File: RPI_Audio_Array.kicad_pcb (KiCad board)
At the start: 2 copper layers, 40 parts, among them J1 Conn_02x20_Odd_Even, U1 PCMD3140IRTER, U2 SPH0690LM4H-1, U3 SPH0690LM4H-1, U4 SPH0690LM4H-1, U5 SPH0690LM4H-1, U6 TLV7103318QDSERQ1

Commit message: Fix: Schemtatic fixes
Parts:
- added C21: 2.2uf, Capacitor_SMD:C_0805_2012Metric, F.Cu at (40.0, 84.4)
- added C22: 2.2uf, Capacitor_SMD:C_0805_2012Metric, F.Cu at (40.2, 67.1)
- added C23: 2.2uf, Capacitor_SMD:C_0805_2012Metric, F.Cu at (40.1, 51.6)
- added C24: 2.2uf, Capacitor_SMD:C_0805_2012Metric, F.Cu at (40.6, 37.2)
- added C25: 2.2uf, Capacitor_SMD:C_0805_2012Metric, F.Cu at (64.0, 54.1)
- added C26: 100nf, Capacitor_SMD:C_1206_3216Metric, F.Cu at (71.5, 45.2)
- added C27: 1nf, Capacitor_SMD:C_0805_2012Metric, F.Cu at (67.8, 45.7)
- added C28: 100pf, Capacitor_SMD:C_0805_2012Metric, F.Cu at (65.5, 45.8)
- added C29: 10uf, Capacitor_SMD:C_1206_3216Metric, F.Cu at (74.3, 45.2)
- added R3: 470, Resistor_SMD:R_0201_0603Metric, F.Cu at (70.3, 52.3)
- added R5: 470, Resistor_SMD:R_0201_0603Metric, F.Cu at (68.8, 52.6)
- C13: value 1uf -> 10nf; footprint Capacitor_SMD:C_0603_1608Metric -> Capacitor_SMD:C_01005_0402Metric
- moved J1 45.8 mm to (83.3, 76.1), turned to 180 degrees
- moved C13 4.33 mm to (69.6, 45.8), turned to 90 degrees
- moved C16 3.52 mm to (62.4, 57.0), turned to -90 degrees
- moved C14 3.10 mm to (66.0, 48.5)
- moved R4 2.93 mm to (70.0, 60.3), turned to 90 degrees
- moved C18 2.28 mm to (66.7, 53.4), turned to 180 degrees
- moved C20 2.08 mm to (66.8, 51.1), turned to 90 degrees
- moved FB1 1.92 mm to (64.3, 51.2), turned to -90 degrees
- moved C17 1.42 mm to (64.0, 56.5), turned to -90 degrees
- moved C15 1.16 mm to (61.4, 50.8)
- moved C19 0.74 mm to (65.0, 56.5), turned to 90 degrees
- moved U6 0.66 mm to (63.0, 47.6)
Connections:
- net GPIO1 renamed PCMD_GPIO1
- C14 pad 1: AVDD -> IOVDD
- FB1 pad 1: AVDD -> IOVDD
- FB1 pad 2: GND -> AVDD
- U1 pad 9: AVDD -> IOVDD
- U2 pad 2: VDD -> IOVDD
- U4 pad 2: VDD -> IOVDD
- U6 pad 6: AVDD -> IOVDD
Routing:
- net PDMCLK: track 134.0 -> 13.9 mm
- net PDM_IN_2: track 69.0 -> 2.48 mm
- net PDM_IN_1: track 65.7 -> 2.69 mm
- net +5V: track 27.1 -> 50.5 mm
- net IOVDD: track 0.00 -> 22.5 mm, vias 0 -> 4
- net AVDD: track 15.5 -> 4.16 mm, vias 2 -> 0
- net SDOUT: track 23.4 -> 33.7 mm, vias 0 -> 2
- net FSYNC: track 27.8 -> 35.8 mm, vias 0 -> 1
- net SCL: track 27.3 -> 34.4 mm, vias 0 -> 1
- net PCMD_GPIO1: track 26.9 -> 20.9 mm, vias 0 -> 2
- net SDA: track 30.7 -> 35.3 mm, vias 0 -> 1
- net FBCLK: track 17.1 -> 13.4 mm
- net DREG: track 4.75 -> 2.46 mm
- net Net-(U2-VDD): track 7.36 -> 9.25 mm
- net GND: track 3.80 -> 5.36 mm, vias 10 -> 26
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
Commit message: Feat: Rerouting PCB
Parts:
- added C30: 10uf, Capacitor_SMD:C_1206_3216Metric, F.Cu at (54.3, 68.6)
- added C31: 100nf, Capacitor_SMD:C_1206_3216Metric, F.Cu at (54.3, 73.1)
- added C32: 10nf, Capacitor_SMD:C_01005_0402Metric, F.Cu at (55.5, 74.9)
- added C33: 1nf, Capacitor_SMD:C_0805_2012Metric, F.Cu at (54.8, 76.6)
- added C34: 100pf, Capacitor_SMD:C_0805_2012Metric, F.Cu at (54.8, 78.9)
- added C36: 100nf, Capacitor_SMD:C_1206_3216Metric, F.Cu at (61.4, 60.3)
- C25: value 2.2uf -> 100nf; footprint Capacitor_SMD:C_0805_2012Metric -> Capacitor_SMD:C_1206_3216Metric
- R3, R5: value 470 -> 4K7
- moved C13 29.8 mm to (60.1, 74.0), turned to 0 degrees
- moved U6 27.4 mm to (65.1, 74.9), turned to 180 degrees
- moved C28 27.0 mm to (60.9, 72.3), turned to 0 degrees
- moved C27 25.3 mm to (60.8, 70.0), turned to 0 degrees
- moved FB1 24.6 mm to (60.8, 75.6), turned to 180 degrees
- moved C26 24.5 mm to (61.4, 67.5), turned to 0 degrees
- moved R10 23.6 mm to (50.8, 58.0), turned to 0 degrees
- moved R11 22.8 mm to (51.1, 55.6), turned to 0 degrees
- moved R12 22.2 mm to (51.8, 53.2), turned to 0 degrees
- moved C29 21.9 mm to (61.4, 62.9), turned to 0 degrees
- moved C15 21.0 mm to (55.0, 70.8)
- moved R3 18.9 mm to (54.3, 62.3), turned to -90 degrees
- moved C14 17.5 mm to (60.6, 65.2)
- moved R5 16.9 mm to (55.3, 62.7), turned to -90 degrees
- moved R4 15.7 mm to (55.8, 53.7), turned to -90 degrees
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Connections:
- net +1V8 renamed FILTER_BANK_1
- C1 pad 1: Net-(U4-VDD) -> SELECT_1
- C11 pad 1: Net-(U4-VDD) -> SELECT_1
- C13 pad 1: +5V -> AVDD
- C14 pad 1: IOVDD -> AVDD
- C22 pad 1: Net-(U4-VDD) -> SELECT_1
- C24 pad 1: Net-(U2-VDD) -> SELECT_2
- C25 pad 1: AVDD -> IOVDD
- C26 pad 1: +5V -> AVDD
- C27 pad 1: +5V -> AVDD
- C28 pad 1: +5V -> AVDD
- C29 pad 1: +5V -> AVDD
- C6 pad 1: Net-(U2-VDD) -> SELECT_2
- C7 pad 1: Net-(U2-VDD) -> SELECT_2
- C8 pad 1: Net-(U2-VDD) -> SELECT_2
- C9 pad 1: Net-(U4-VDD) -> SELECT_1
- FB2 pad 1: Net-(U2-VDD) -> SELECT_2
- FB4 pad 1: Net-(U4-VDD) -> SELECT_1
- U2 pad 2: IOVDD -> SELECT_2
- U2 pad 5: Net-(U2-VDD) -> SELECT_2
- U4 pad 2: IOVDD -> SELECT_1
- U4 pad 5: Net-(U4-VDD) -> SELECT_1
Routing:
- net FBCLK: track 13.4 -> 90.9 mm, vias 0 -> 1
- net PCMD_GPIO1: track 20.9 -> 60.1 mm, vias 2 -> 1
- net SDA: track 35.3 -> 71.1 mm
- net FSYNC: track 35.8 -> 69.6 mm
- net SCL: track 34.4 -> 67.2 mm
- net GND: track 5.36 -> 37.9 mm, vias 26 -> 35
- net FILTER_BANK_1: track 4.41 -> 28.0 mm, vias 1 -> 3
- net SDOUT: track 33.7 -> 51.0 mm, vias 2 -> 1
- net +5V: track 50.5 -> 35.1 mm
- net AVDD: track 4.16 -> 18.1 mm
- net IOVDD: track 22.5 -> 31.8 mm, vias 4 -> 0
- net SELECT_2: track 0.00 -> 9.25 mm
- net Net-(U2-VDD): track 9.25 -> 0.00 mm
- net SELECT_1: track 0.00 -> 7.18 mm
- net Net-(U4-VDD): track 7.18 -> 0.00 mm
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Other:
- board text added: "To place grounds"

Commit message: Feat: adding more routing
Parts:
- moved J1 45.7 mm to (90.4, 121.3)
- moved FB5 39.6 mm to (43.4, 120.9)
- moved R9 39.2 mm to (36.8, 118.4)
- moved U5 39.2 mm to (31.8, 119.8)
- moved C4 38.1 mm to (40.7, 121.4)
- moved C21 37.7 mm to (35.2, 121.9)
- moved C10 37.6 mm to (39.1, 121.7)
- moved C12 37.4 mm to (37.2, 121.7)
- moved C15 35.7 mm to (63.9, 105.4)
- moved C17 35.7 mm to (71.4, 92.5)
- moved C20 35.7 mm to (66.7, 97.4)
- moved C30 35.7 mm to (63.2, 103.2)
- moved C31 35.7 mm to (63.2, 107.7)
- moved C33 35.7 mm to (63.7, 111.2)
- moved FB1 35.7 mm to (69.7, 110.2)
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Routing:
- net PDMCLK: track 13.9 -> 170.4 mm, vias 0 -> 5
- net FILTER_BANK_1: track 28.0 -> 170.7 mm, vias 3 -> 8
- net PDM_IN_2: track 2.99 -> 123.5 mm, vias 3 -> 0
- net PDM_IN_1: track 3.76 -> 111.6 mm, vias 3 -> 0
- net GND: track 37.9 -> 59.8 mm, vias 35 -> 291
- net FSYNC: track 69.6 -> 78.4 mm
- net FBCLK: track 90.9 -> 83.9 mm, vias 1 -> 2
- net SELECT_1: track 7.18 -> 13.9 mm
- net SDOUT: track 51.0 -> 57.6 mm
- net SCL: track 67.2 -> 62.0 mm
- net PCMD_GPIO1: track 60.1 -> 65.2 mm
- net SELECT_2: track 9.25 -> 12.3 mm
- net Net-(U3-VDD): track 7.10 -> 9.52 mm
- net Net-(U5-VDD): track 7.49 -> 9.87 mm
- net +5V: track 35.1 -> 33.3 mm
- added copper zone on F.Cu, net GND
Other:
- board outline added: 66.9 x 99.2 mm
- board text removed: "To place grounds"

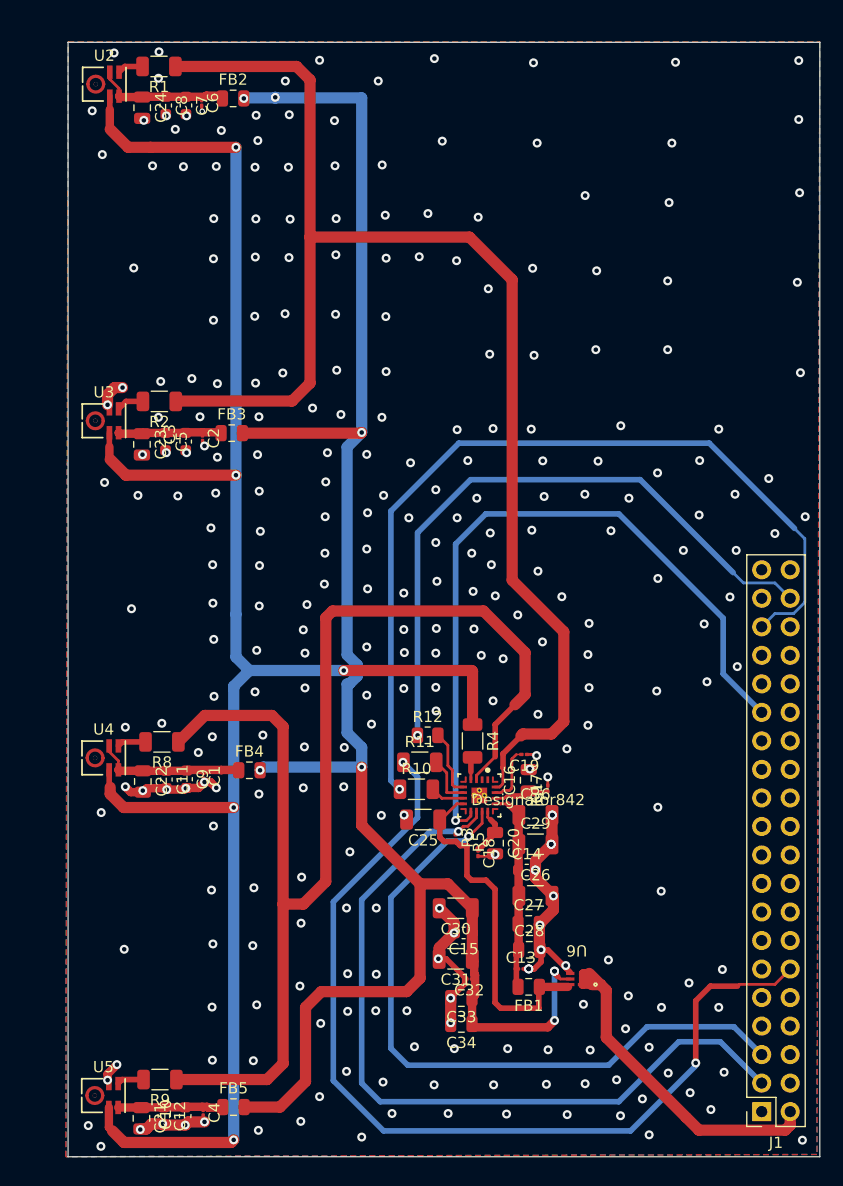
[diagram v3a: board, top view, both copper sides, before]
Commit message: Chore: To fix drc issues
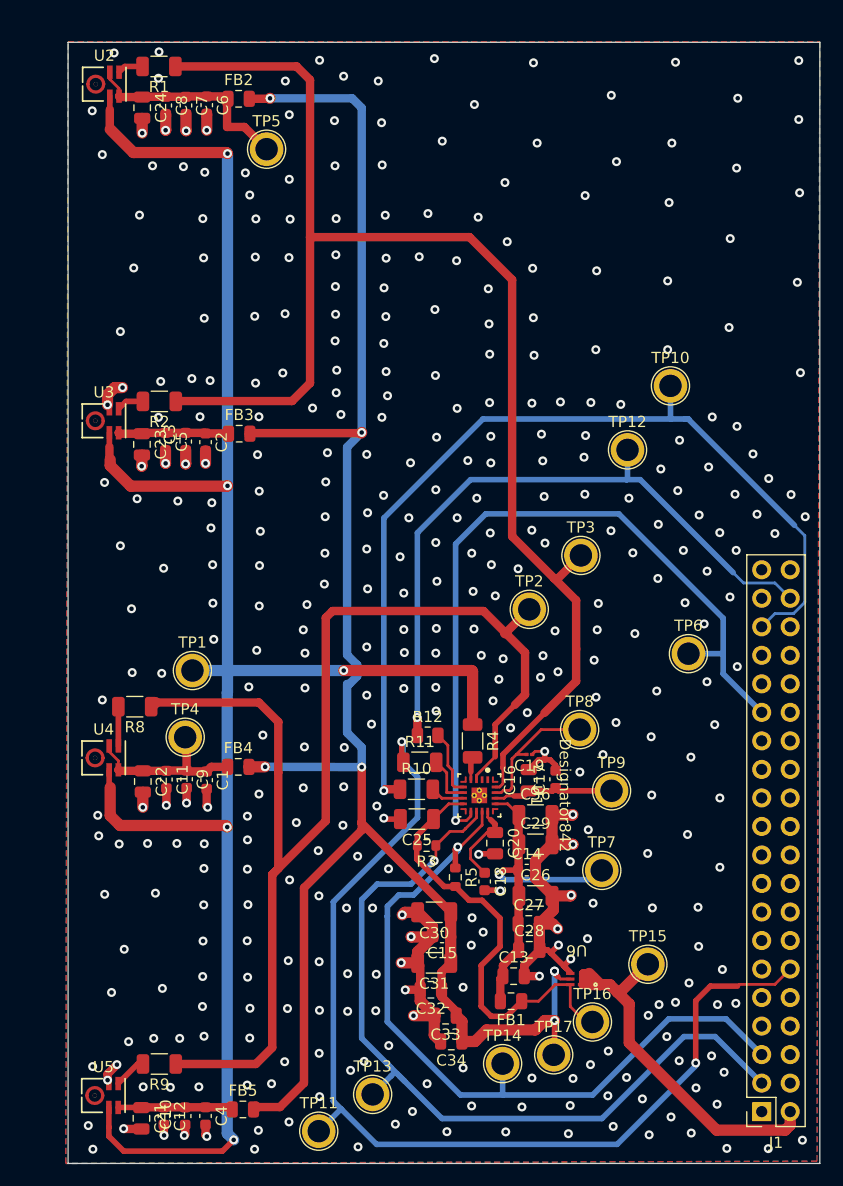
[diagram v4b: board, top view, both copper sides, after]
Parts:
- added TP1: TestPoint, TestPoint:TestPoint_Plated_Hole_D2.0mm, F.Cu at (39.7, 82.0)
- added TP10: TestPoint, TestPoint:TestPoint_Plated_Hole_D2.0mm, F.Cu at (82.3, 56.6)
- added TP11: TestPoint, TestPoint:TestPoint_Plated_Hole_D2.0mm, F.Cu at (51.0, 123.0)
- added TP12: TestPoint, TestPoint:TestPoint_Plated_Hole_D2.0mm, F.Cu at (78.5, 62.4)
- added TP13: TestPoint, TestPoint:TestPoint_Plated_Hole_D2.0mm, F.Cu at (55.8, 119.8)
- added TP14: TestPoint, TestPoint:TestPoint_Plated_Hole_D2.0mm, F.Cu at (67.3, 117.0)
- added TP15: TestPoint, TestPoint:TestPoint_Plated_Hole_D2.0mm, F.Cu at (80.3, 108.2)
- added TP16: TestPoint, TestPoint:TestPoint_Plated_Hole_D2.0mm, F.Cu at (75.3, 113.3)
- added TP17: TestPoint, TestPoint:TestPoint_Plated_Hole_D2.0mm, F.Cu at (71.9, 116.2)
- added TP2: TestPoint, TestPoint:TestPoint_Plated_Hole_D2.0mm, F.Cu at (69.7, 76.5)
- added TP3: TestPoint, TestPoint:TestPoint_Plated_Hole_D2.0mm, F.Cu at (74.3, 71.8)
- added TP4: TestPoint, TestPoint:TestPoint_Plated_Hole_D2.0mm, F.Cu at (39.1, 87.9)
- added TP5: TestPoint, TestPoint:TestPoint_Plated_Hole_D2.0mm, F.Cu at (46.3, 35.6)
- added TP6: TestPoint, TestPoint:TestPoint_Plated_Hole_D2.0mm, F.Cu at (83.9, 80.5)
- added TP7: TestPoint, TestPoint:TestPoint_Plated_Hole_D2.0mm, F.Cu at (76.2, 99.8)
- added TP8: TestPoint, TestPoint:TestPoint_Plated_Hole_D2.0mm, F.Cu at (74.2, 87.3)
- added TP9: TestPoint, TestPoint:TestPoint_Plated_Hole_D2.0mm, F.Cu at (77.0, 92.7)
- C1, C17, C18, C2, C4, C6: footprint Capacitor_SMD:C_01005_0402Metric -> Capacitor_SMD:C_0603_1608Metric
- C13, C32: footprint Capacitor_SMD:C_01005_0402Metric -> Capacitor_SMD:C_0805_2012Metric
- R3, R5: footprint Resistor_SMD:R_0201_0603Metric -> Resistor_SMD:R_0603_1608Metric
- moved R8 3.96 mm to (34.6, 85.2)
- moved C32 3.55 mm to (61.0, 110.4)
- moved R5 3.30 mm to (63.1, 100.4)
- moved R3 2.69 mm to (60.6, 97.6), turned to 180 degrees
- moved C18 2.59 mm to (65.8, 100.8)
- moved C33 2.10 mm to (62.3, 112.7)
- moved FB1 2.03 mm to (68.1, 111.5)
- moved C15 1.95 mm to (62.0, 105.7)
- moved C30 1.95 mm to (61.3, 103.5)
- moved C31 1.95 mm to (61.3, 108.0)
- moved C34 1.80 mm to (62.8, 115.0)
- moved R9 1.38 mm to (36.8, 117.0)
- moved C17 1.07 mm to (72.1, 91.7)
- moved FB4 1.04 mm to (43.8, 90.6)
- moved C13 0.91 mm to (68.3, 109.2)
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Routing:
- net GND: track 59.8 -> 88.9 mm, vias 291 -> 383
- net AVDD: track 18.1 -> 31.6 mm, vias 0 -> 1
- net FBCLK: track 83.9 -> 92.6 mm
- net SELECT_2: track 12.3 -> 19.8 mm
- net IOVDD: track 31.8 -> 38.9 mm
- net VREF: track 5.31 -> 12.3 mm
- net FSYNC: track 78.4 -> 85.2 mm
- net SCL: track 62.0 -> 68.1 mm
- net AREG: track 5.01 -> 10.9 mm
- net PDMCLK: track 170.4 -> 175.9 mm
- net DREG: track 4.37 -> 7.71 mm
- net +5V: track 33.3 -> 36.6 mm
- net PCMD_GPIO1: track 65.2 -> 68.3 mm
- net SDA: track 70.9 -> 73.9 mm
- net SDOUT: track 57.6 -> 60.3 mm
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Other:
- board size 66.9 x 99.2 mm -> 66.9 x 99.9 mm

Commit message: Feat: Resolving all DRC warnings
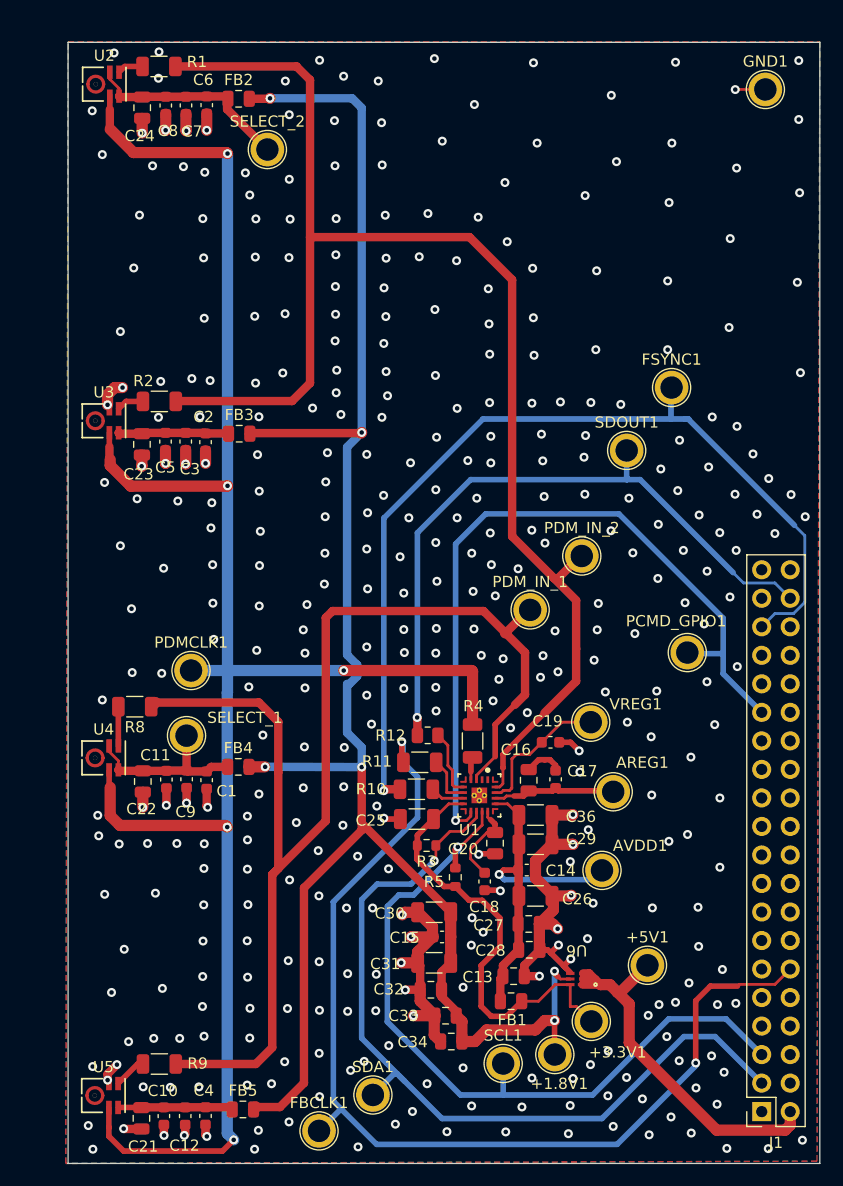
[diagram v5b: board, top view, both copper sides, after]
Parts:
- removed TP1, TP10, TP11, TP12, TP13, TP14, TP15, TP16, TP17, TP2, TP3, TP4, TP5, TP6, TP7, TP8, TP9: TestPoint, TestPoint:TestPoint_Plated_Hole_D2.0mm
- added +1.8V1: TestPoint, TestPoint:TestPoint_Plated_Hole_D2.0mm, F.Cu at (72.0, 116.2)
- added +3.3V1: TestPoint, TestPoint:TestPoint_Plated_Hole_D2.0mm, F.Cu at (75.2, 113.2)
- added +5V1: TestPoint, TestPoint:TestPoint_Plated_Hole_D2.0mm, F.Cu at (80.2, 108.2)
- added AREG1: TestPoint, TestPoint:TestPoint_Plated_Hole_D2.0mm, F.Cu at (77.2, 92.8)
- added AVDD1: TestPoint, TestPoint:TestPoint_Plated_Hole_D2.0mm, F.Cu at (76.2, 99.8)
- added FBCLK1: TestPoint, TestPoint:TestPoint_Plated_Hole_D2.0mm, F.Cu at (51.0, 123.0)
- added FSYNC1: TestPoint, TestPoint:TestPoint_Plated_Hole_D2.0mm, F.Cu at (82.4, 56.8)
- added GND1: TestPoint, TestPoint:TestPoint_Plated_Hole_D2.0mm, F.Cu at (90.8, 30.2)
- added PCMD_GPIO1: TestPoint, TestPoint:TestPoint_Plated_Hole_D2.0mm, F.Cu at (83.8, 80.4)
- added PDMCLK1: TestPoint, TestPoint:TestPoint_Plated_Hole_D2.0mm, F.Cu at (39.6, 82.0)
- added PDM_IN_1: TestPoint, TestPoint:TestPoint_Plated_Hole_D2.0mm, F.Cu at (69.8, 76.6)
- added PDM_IN_2: TestPoint, TestPoint:TestPoint_Plated_Hole_D2.0mm, F.Cu at (74.4, 71.8)
- added SCL1: TestPoint, TestPoint:TestPoint_Plated_Hole_D2.0mm, F.Cu at (67.4, 117.0)
- added SDA1: TestPoint, TestPoint:TestPoint_Plated_Hole_D2.0mm, F.Cu at (55.8, 119.8)
- added SDOUT1: TestPoint, TestPoint:TestPoint_Plated_Hole_D2.0mm, F.Cu at (78.4, 62.4)
- added SELECT_1: TestPoint, TestPoint:TestPoint_Plated_Hole_D2.0mm, F.Cu at (39.2, 87.8)
- added SELECT_2: TestPoint, TestPoint:TestPoint_Plated_Hole_D2.0mm, F.Cu at (46.4, 35.6)
- added VREG1: TestPoint, TestPoint:TestPoint_Plated_Hole_D2.0mm, F.Cu at (75.2, 86.6)
- C19: footprint Capacitor_SMD:C_01005_0402Metric -> Capacitor_SMD:C_0603_1608Metric
- moved C19 2.18 mm to (71.6, 88.4)
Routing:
- net GND: track 88.9 -> 91.8 mm, vias 383 -> 382
- net +5V: track 36.6 -> 34.6 mm
- net SELECT_2: track 19.8 -> 18.4 mm
- net FILTER_BANK_1: track 169.2 -> 169.1 mm, vias 7 -> 6
